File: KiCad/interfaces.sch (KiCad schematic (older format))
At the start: 24 parts

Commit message: Clean artefaccs, clean space for new DCDC
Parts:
- SP7: footprint jetson-nano-baseboard-footprints:M2.5-4mm -> antmicro-footprints:9774060151
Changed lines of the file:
@@
 F 0 "SP7" H 5625 9075 60  0000 R TNN
 F 1 "9774040151" H 5600 9175 60  0000 R TNN
-F 2 "jetson-nano-baseboard-footprints:M2.5-4mm" H 5600 9500 60  0001 C CNN
+F 2 "antmicro-footprints:9774060151" H 5600 9500 60  0001 C CNN
 F 3 "" H 5600 9500 60  0001 C CNN
 F 4 "Wurth Elektronik" H 5500 9300 50  0001 C CNN "Manufacturer"

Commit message: Move ethernet connector closet to the edge. Loclib
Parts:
- SP7: footprint antmicro-footprints:9774060151 -> jetson-nano-baseboard-footprints:9774060151
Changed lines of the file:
@@
 F 0 "SP7" H 5625 9075 60  0000 R TNN
 F 1 "9774040151" H 5600 9175 60  0000 R TNN
-F 2 "antmicro-footprints:9774060151" H 5600 9500 60  0001 C CNN
+F 2 "jetson-nano-baseboard-footprints:9774060151" H 5600 9500 60  0001 C CNN
 F 3 "" H 5600 9500 60  0001 C CNN
 F 4 "Wurth Elektronik" H 5500 9300 50  0001 C CNN "Manufacturer"

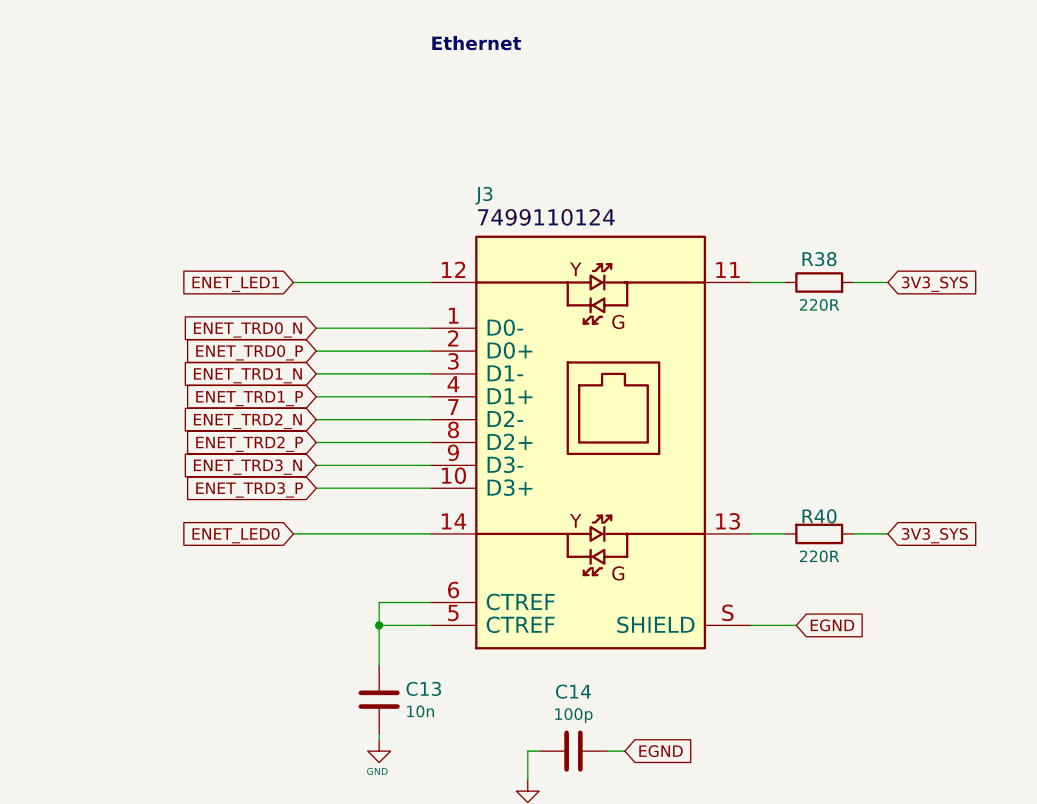
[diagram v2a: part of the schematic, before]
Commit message: Replace ethernet connector, fix traces and tuning
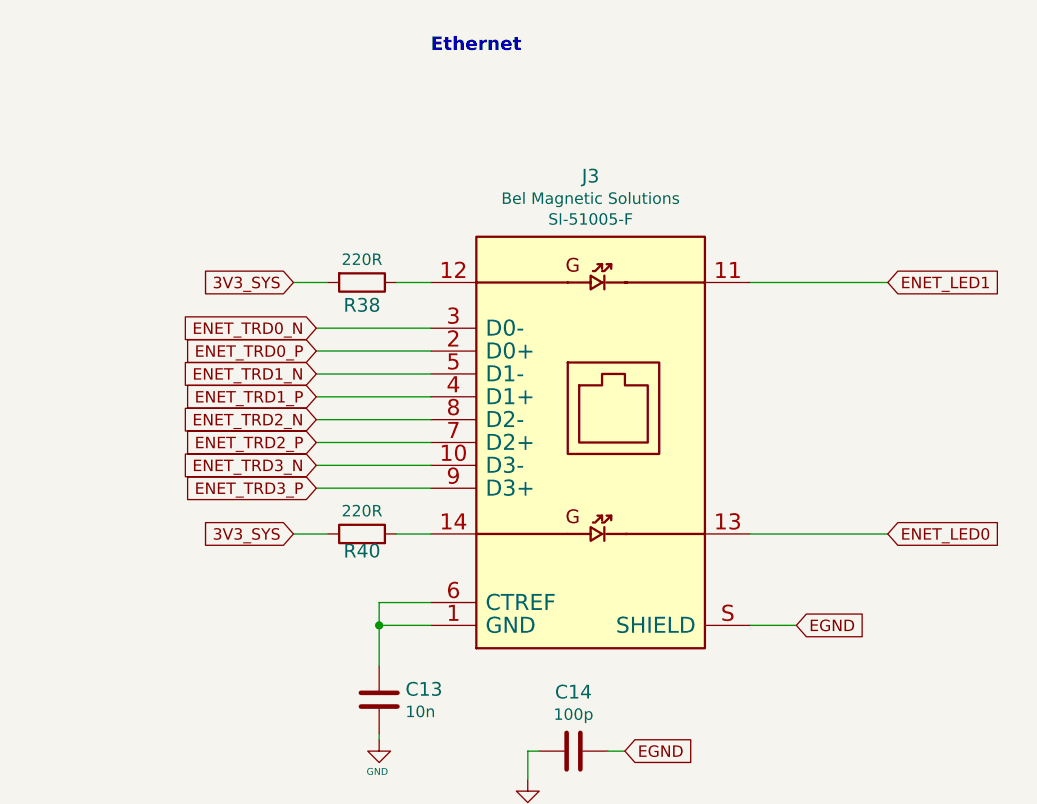
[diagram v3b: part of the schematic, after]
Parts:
- removed J3: ~, jetson-nano-baseboard-footprints:WE_7499110124, symbol jetson-nano-baseboard:WE_7499111447
- added J3: SI-51005-F, jetson-nano-baseboard-footprints:SI-51005-F, symbol jetson-nano-baseboard:SI-51005-F
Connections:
- net EGND: now also J3.S (SHIELD)
- net ENET_LED0: now also J3.13
- net ENET_LED1: now also J3.11
- net ENET_TRD0_N: now also J3.3 (D0-)
- net ENET_TRD0_P: now also J3.2 (D0+)
- net ENET_TRD1_N: now also J3.5 (D1-)
- net ENET_TRD1_P: now also J3.4 (D1+)
- net ENET_TRD2_N: now also J3.8 (D2-)
- net ENET_TRD2_P: now also J3.7 (D2+)
- net ENET_TRD3_N: now also J3.10 (D3-)
- net ENET_TRD3_P: now also J3.9 (D3+)
- net at R38.1: now also J3.12
- net at R40.2: now also J3.14
- net at C13.1: now also J3.1 (GND), J3.6 (CTREF)
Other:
- moved on the sheet: R38, R40
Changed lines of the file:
@@
 Text Notes 11825 4300 0    59   ~ 12
 Ethernet
-Text Label 12025 5075 0    70   ~ 0
-7499110124
 Text Notes 4783 4310 0    59   ~ 12
 M.2 NVMe Interface
@@
 Text Label 4893 4739 0    70   ~ 0
 MDT580M01001
-Text GLabel 13825 5300 2    50   Input ~ 0
-3V3_SYS
-Text GLabel 13825 6400 2    50   Input ~ 0
+Text GLabel 11225 6400 0    50   Input ~ 0
 3V3_SYS
 Text GLabel 3175 4750 1    50   Input ~ 0
@@
 $EndComp
 $Comp
-L jetson-nano-baseboard:WE_7499111447 J3
-U 1 1 5E710433
-P 12525 6200
-F 0 "J3" H 12025 7450 60  0000 L BNN
-F 1 "~" H 12525 6200 50  0001 C CNN
-F 2 "jetson-nano-baseboard-footprints:WE_7499110124" H 12525 6200 50  0001 C CNN
-F 3 "" H 12525 6200 50  0001 C CNN
-F 4 "Wurth Elektronik" V 675 4907 60  0001 C CNN "Manufacturer"
-F 5 "7499110124" V 675 4907 60  0001 C CNN "PartSymbol"
-F 6 "7499111447" H -31358 940 50  0001 C CNN "MPN"
-	1    12525 6200
-	1    0    0    -1
-$EndComp
-$Comp
 L jetson-nano-baseboard:LED NVME1
 U 1 1 5E710432
@@
 	11325 6200 11825 6200
 Wire Wire Line
-	11825 6400 11225 6400
-Wire Wire Line
-	11825 5300 11225 5300
+	13225 6400 13825 6400
+Wire Wire Line
+	13225 5300 13825 5300
 Wire Wire Line
 	13225 6800 13425 6800
@@
 Text GLabel 11325 6200 0    50   Input ~ 0
 ENET_TRD3_P
-Text GLabel 11225 5300 0    50   Input ~ 0
+Text GLabel 13825 5300 2    50   Input ~ 0
 ENET_LED1
-Text GLabel 11225 6400 0    50   Input ~ 0
+Text GLabel 13825 6400 2    50   Input ~ 0
 ENET_LED0
 $Comp
@@
 	9225 9375 9225 9450
 $Comp
-L jetson-nano-baseboard:R_220R_0402 R38
-U 1 1 62BC9C4E
-P 13525 5300
-F 0 "R38" H 13525 5400 60  0000 C CNN
-F 1 "R_220R_0402" H 13525 5150 60  0001 C CNN
-F 2 "jetson-nano-baseboard-footprints:0402-res" H 13725 5500 60  0001 L CNN
-F 3 "" H 13525 5300 50  0001 C CNN
-F 4 "Panasonic" H 13725 5700 60  0001 L CNN "Manufacturer"
-F 5 "ERJ2GEJ221X" H 13725 5600 60  0001 L CNN "MPN"
-F 6 "220R" H 13525 5200 50  0000 C CNN "Val"
-	1    13525 5300
-	1    0    0    -1
-$EndComp
-$Comp
 L jetson-nano-baseboard:R_220R_0402 R40
 U 1 1 62BCA909
-P 13525 6400
-F 0 "R40" H 13525 6325 60  0000 C CNN
-F 1 "R_220R_0402" H 13525 6250 60  0001 C CNN
-F 2 "jetson-nano-baseboard-footprints:0402-res" H 13725 6600 60  0001 L CNN
-F 3 "" H 13525 6400 50  0001 C CNN
-F 4 "Panasonic" H 13725 6800 60  0001 L CNN "Manufacturer"
-F 5 "ERJ2GEJ221X" H 13725 6700 60  0001 L CNN "MPN"
-F 6 "220R" H 13525 6500 50  0000 C CNN "Val"
-	1    13525 6400
-	-1   0    0    1
-$EndComp
-Wire Wire Line
-	13675 6400 13825 6400
-Wire Wire Line
-	13225 6400 13375 6400
-Wire Wire Line
-	13225 5300 13375 5300
-Wire Wire Line
-	13675 5300 13825 5300
+P 11525 6400
+F 0 "R40" H 11525 6325 60  0000 C CNN
+F 1 "R_220R_0402" H 11525 6250 60  0001 C CNN
+F 2 "jetson-nano-baseboard-footprints:0402-res" H 11725 6600 60  0001 L CNN
+F 3 "" H 11525 6400 50  0001 C CNN
+F 4 "Panasonic" H 11725 6800 60  0001 L CNN "Manufacturer"
+F 5 "ERJ2GEJ221X" H 11725 6700 60  0001 L CNN "MPN"
+F 6 "220R" H 11525 6500 50  0000 C CNN "Val"
+	1    11525 6400
+	1    0    0    -1
+$EndComp
+Wire Wire Line
+	11375 6400 11225 6400
+Wire Wire Line
+	11825 6400 11675 6400
+Wire Wire Line
+	11825 5300 11675 5300
 $Comp
 L jetson-nano-baseboard:C_100p_0402 C14
@@
 Wire Wire Line
 	7600 7800 8400 7800
+$Comp
+L jetson-nano-baseboard:SI-51005-F J3
+U 1 1 61B50EDA
+P 12525 6200
+F 0 "J3" H 12525 7565 60  0000 C CNN
+F 1 "SI-51005-F" H 12525 7383 60  0001 C CNN
+F 2 "jetson-nano-baseboard-footprints:SI-51005-F" H 12525 5250 60  0001 C CNN
+F 3 "https://belfuse.com/resources/drawings/magneticsolutions/dr-mag-si-51005-fb.pdf" H 12525 6200 60  0001 C CNN
+F 4 "Bel Magnetic Solutions " H 12525 7467 50  0000 C CNN "Manufacturer"
+F 5 "SI-51005-F " H 12525 7376 50  0000 C CNN "MPN"
+	1    12525 6200
+	1    0    0    -1
+$EndComp
+Wire Wire Line
+	11375 5300 11225 5300
+$Comp
+L jetson-nano-baseboard:R_220R_0402 R38
+U 1 1 62BC9C4E
+P 11525 5300
+F 0 "R38" H 11525 5400 60  0000 C CNN
+F 1 "R_220R_0402" H 11525 5150 60  0001 C CNN
+F 2 "jetson-nano-baseboard-footprints:0402-res" H 11725 5500 60  0001 L CNN
+F 3 "" H 11525 5300 50  0001 C CNN
+F 4 "Panasonic" H 11725 5700 60  0001 L CNN "Manufacturer"
+F 5 "ERJ2GEJ221X" H 11725 5600 60  0001 L CNN "MPN"
+F 6 "220R" H 11525 5200 50  0000 C CNN "Val"
+	1    11525 5300
+	-1   0    0    1
+$EndComp
+Text GLabel 11225 5300 0    50   Input ~ 0
+3V3_SYS
 $EndSCHEMATC

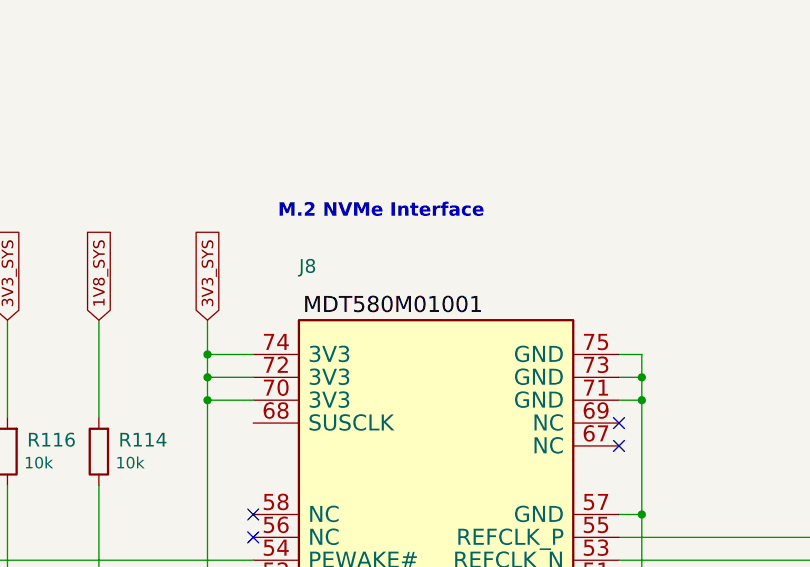
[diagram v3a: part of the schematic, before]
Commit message: MDT580M01001 -> 1-2199230-6
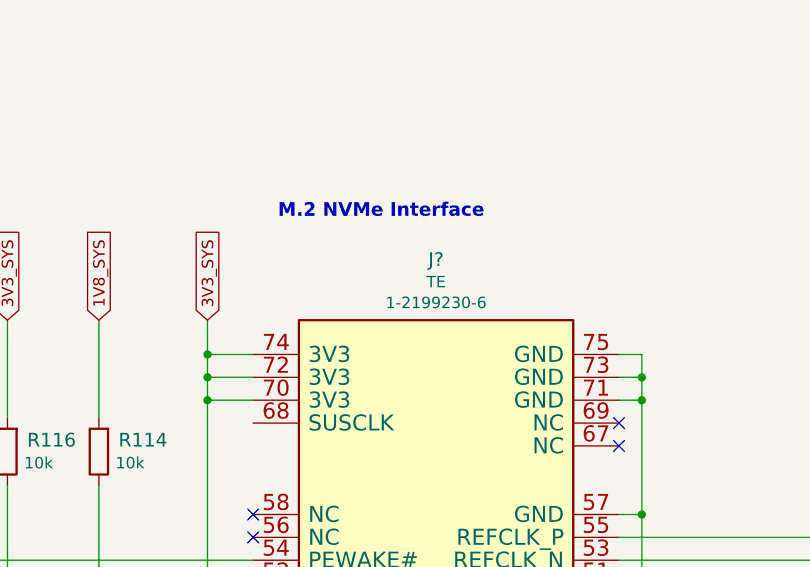
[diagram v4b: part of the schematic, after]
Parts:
- removed J8: ~, jetson-nano-baseboard-footprints:MDT580M01001, symbol jetson-nano-baseboard:MDT580M01001
- added J?: 1-2199230-6, antmicro-footprints:1-2199230-6, symbol antmicroPciConnectors:1-2199230-6
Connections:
- net 3V3_SYS: now also J?.12 (3V3), J?.14 (3V3), J?.16 (3V3), J?.18 (3V3), J?.2 (3V3), J?.4 (3V3), J?.70 (3V3), J?.72 (3V3), J?.74 (3V3)
- net C_PCIE0_TX0_N: now also J?.47 (PET0_N)
- net C_PCIE0_TX0_P: now also J?.49 (PET0_P)
- net C_PCIE0_TX1_N: now also J?.35 (PET1_N)
- net C_PCIE0_TX1_P: now also J?.37 (PET1_P)
- net C_PCIE0_TX2_N: now also J?.23 (PET2_N)
- net C_PCIE0_TX2_P: now also J?.25 (PET2_P)
- net C_PCIE0_TX3_N: now also J?.11 (PET3_N)
- net C_PCIE0_TX3_P: now also J?.13 (PET3_P)
- net GND: now also J?.1 (GND), J?.15 (GND), J?.21 (GND), J?.27 (GND), J?.3 (GND), J?.33 (GND), J?.39 (GND), J?.45 (GND), J?.51 (GND), J?.57 (GND), J?.71 (GND), J?.73 (GND), J?.75 (GND), J?.9 (GND), J?.SH1 (SHIELD), J?.SH2 (SHIELD)
- net M2_ALERT: now also J?.44 (ALERT)
- net PCIE0_CLK_N: now also J?.53 (REFCLK_N)
- net PCIE0_CLK_P: now also J?.55 (REFCLK_P)
- net PCIE0_RX0_N: now also J?.41 (PER0_N)
- net PCIE0_RX0_P: now also J?.43 (PER0_P)
- net PCIE0_RX1_N: now also J?.29 (PER1_N)
- net PCIE0_RX1_P: now also J?.31 (PER1_P)
- net PCIE0_RX2_N: now also J?.17 (PER2_N)
- net PCIE0_RX2_P: now also J?.19 (PER2_P)
- net PCIE0_RX3_N: now also J?.5 (PER3_N)
- net PCIE0_RX3_P: now also J?.7 (PER3_P)
- net PEX_L0_CLKREQ_N: now also J?.52 (CLKREQ#)
- net PEX_L0_RST_N: now also J?.50 (PERST#)
- net \PEWAKE_3V3: now also J?.54 (PEWAKE#)
- net at TP20.1 (P): now also J?.40 (SMB_CLK)
- net at TP7.1 (P): now also J?.42 (SMB_DATA)
- net at NVME1.K: now also J?.10 (LED)
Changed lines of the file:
@@
 Text Label 6575 7800 0    60   ~ 0
 C_PCIE0_TX3_P
-Text Label 4893 4739 0    70   ~ 0
-MDT580M01001
 Text GLabel 11225 6400 0    50   Input ~ 0
 3V3_SYS
@@
 $EndComp
 $Comp
-L jetson-nano-baseboard:9774040151 SP7
-U 1 1 5E710438
-P 5500 9300
-F 0 "SP7" H 5625 9075 60  0000 R TNN
-F 1 "9774040151" H 5600 9175 60  0000 R TNN
-F 2 "jetson-nano-baseboard-footprints:9774060151" H 5600 9500 60  0001 C CNN
-F 3 "" H 5600 9500 60  0001 C CNN
-F 4 "Wurth Elektronik" H 5500 9300 50  0001 C CNN "Manufacturer"
-F 5 "9774040151" H 5500 9300 50  0001 C CNN "MPN"
-	1    5500 9300
-	-1   0    0    1
-$EndComp
-$Comp
 L jetson-nano-baseboard:LED NVME1
 U 1 1 5E710432
@@
 	4475 5000 4475 5100
 Connection ~ 4475 5100
-$Comp
-L jetson-nano-baseboard:MDT580M01001 J8
-U 1 1 5E710439
-P 5475 7150
-F 0 "J8" H 4875 9750 60  0000 L BNN
-F 1 "~" H 5325 5450 60  0000 C CNN
-F 2 "jetson-nano-baseboard-footprints:MDT580M01001" H 5325 5450 60  0001 C CNN
-F 3 "" H 5475 7150 60  0000 C CNN
-F 4 "Amphenol" H 4160 5862 60  0001 C CNN "Manufacturer"
-F 5 "MDT580M01001" H 5194 5434 60  0001 C CNN "MPN"
-	1    5475 7150
-	1    0    0    -1
-$EndComp
 NoConn ~ 4675 5600
 NoConn ~ 4675 5700
@@
 Text GLabel 11225 5300 0    50   Input ~ 0
 3V3_SYS
+$Comp
+L jetson-nano-baseboard:9774040151 SP7
+U 1 1 5E710438
+P 5500 9300
+F 0 "SP7" H 5625 9075 60  0000 R TNN
+F 1 "9774040151" H 5600 9175 60  0000 R TNN
+F 2 "jetson-nano-baseboard-footprints:9774060151" H 5600 9500 60  0001 C CNN
+F 3 "" H 5600 9500 60  0001 C CNN
+F 4 "Wurth Elektronik" H 5500 9300 50  0001 C CNN "Manufacturer"
+F 5 "9774040151" H 5500 9300 50  0001 C CNN "MPN"
+	1    5500 9300
+	-1   0    0    1
+$EndComp
+$Comp
+L antmicroPciConnectors:1-2199230-6 J?
+U 1 1 6246454E
+P 5475 7150
+F 0 "J?" H 5475 9815 60  0000 C CNN
+F 1 "1-2199230-6" H 5325 5450 60  0001 C CNN
+F 2 "antmicro-footprints:1-2199230-6" H 5325 5450 60  0001 C CNN
+F 3 "" H 5325 7150 60  0001 C CNN
+F 4 "TE" H 5475 9717 50  0000 C CNN "Manufacturer"
+F 5 "1-2199230-6" H 5475 9626 50  0000 C CNN "MPN"
+	1    5475 7150
+	1    0    0    -1
+$EndComp
 $EndSCHEMATC

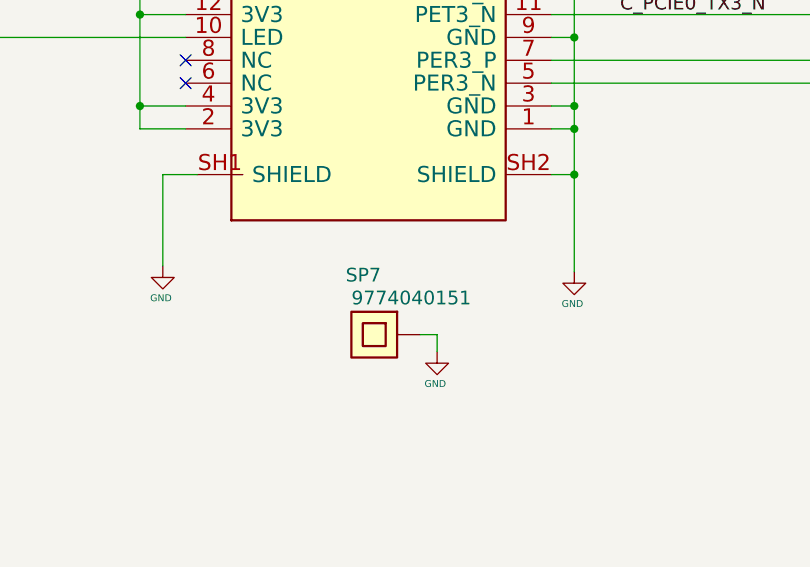
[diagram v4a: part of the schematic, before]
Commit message: 9774040151 -> 9774025151
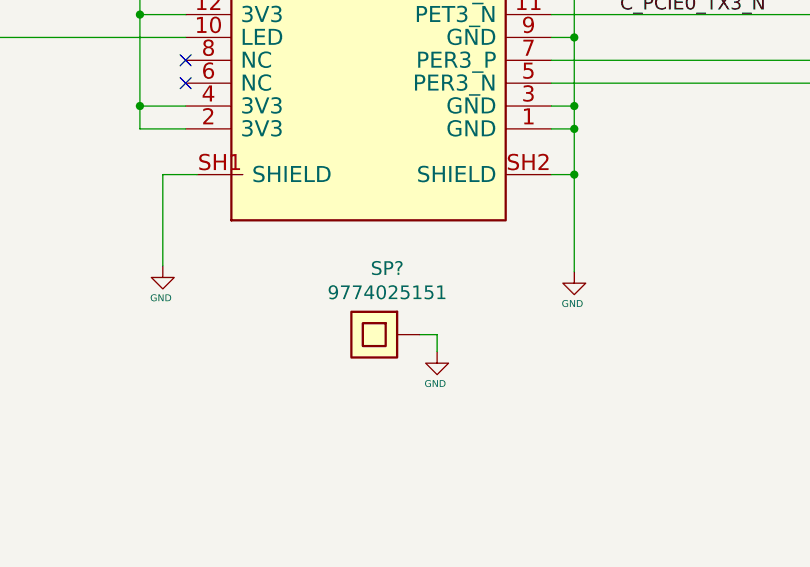
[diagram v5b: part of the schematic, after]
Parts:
- removed SP7: 9774040151, jetson-nano-baseboard-footprints:9774060151, symbol jetson-nano-baseboard:9774040151
- added SP?: 9774025151, antmicro-footprints:9774025151, symbol antmicroMechanicalParts:9774025151
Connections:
- net GND: now also SP?.1
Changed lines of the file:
@@
 3V3_SYS
-$Comp
-L jetson-nano-baseboard:9774040151 SP7
-U 1 1 5E710438
-P 5500 9300
-F 0 "SP7" H 5625 9075 60  0000 R TNN
-F 1 "9774040151" H 5600 9175 60  0000 R TNN
-F 2 "jetson-nano-baseboard-footprints:9774060151" H 5600 9500 60  0001 C CNN
-F 3 "" H 5600 9500 60  0001 C CNN
-F 4 "Wurth Elektronik" H 5500 9300 50  0001 C CNN "Manufacturer"
-F 5 "9774040151" H 5500 9300 50  0001 C CNN "MPN"
-	1    5500 9300
-	-1   0    0    1
-$EndComp
 $Comp
 L antmicroPciConnectors:1-2199230-6 J?
@@
 	1    0    0    -1
 $EndComp
+$Comp
+L antmicroMechanicalParts:9774025151 SP?
+U 1 1 6248F20F
+P 5500 9300
+F 0 "SP?" H 5443 9011 60  0000 C CNN
+F 1 "9774025151" H 5443 9117 60  0000 C CNN
+F 2 "antmicro-footprints:9774025151" H 5500 9300 60  0001 C CNN
+F 3 "" H 5500 9300 60  0001 C CNN
+F 4 "Wurth Elektronik" H 5500 9300 50  0001 C CNN "Manufacturer"
+F 5 "9774025151" H 5500 9300 50  0001 C CNN "MPN"
+	1    5500 9300
+	-1   0    0    1
+$EndComp
 $EndSCHEMATC
